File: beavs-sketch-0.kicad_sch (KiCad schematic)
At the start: 26 parts, among them J1 USB_C_Receptacle_USB2.0_16P, J10 Conn_01x03, J11 Conn_01x03, J2 Conn_Coaxial, J3 Micro_SD_Card_Det2, J4 Conn_Coaxial, J5 Conn_01x02, J6 Conn_01x03, J7 Conn_01x03, J8 Conn_01x03, J9 Conn_01x03, U1 RP2040, U2 W25Q128JVS, U3 MS5607-02BA, U4 RFM95W-915S2, U5 MAX-M10S, Y1 Crystal_GND24

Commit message: do some schematic work
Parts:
- removed C1, C2: C_Small, symbol Device:C_Small
- removed J10, J11, J6, J7, J8, J9: Conn_01x03, Connector_JST:JST_XH_B3B-XH-AM_1x03_P2.50mm_Vertical, symbol Connector_Generic:Conn_01x03
- removed J2: Conn_Coaxial, Connector_Coaxial:U.FL_Molex_MCRF_73412-0110_Vertical, symbol Connector:Conn_Coaxial
- removed J3: Micro_SD_Card_Det2, Connector_Card:microSD_HC_Hirose_DM3AT-SF-PEJM5, symbol Connector:Micro_SD_Card_Det2
- removed R1: 1k, Resistor_SMD:R_0402_1005Metric, symbol Device:R_Small
- removed U1: RP2040, Package_DFN_QFN:QFN-56-1EP_7x7mm_P0.4mm_EP3.2x3.2mm, symbol MCU_RaspberryPi:RP2040
- removed U2: W25Q128JVS, Package_SO:SOIC-8_5.3x5.3mm_P1.27mm, symbol Memory_Flash:W25Q128JVS
- removed U3: MS5607-02BA, Package_LGA:LGA-8_3x5mm_P1.25mm, symbol Sensor_Pressure:MS5607-02BA
- removed U5: MAX-M10S, RF_GPS:ublox_MAX, symbol RF_GPS:MAX-M10S
- removed Y1: Crystal_GND24, Crystal:Crystal_SMD_Abracon_ABM8AIG-4Pin_3.2x2.5mm, symbol Device:Crystal_GND24
- added J3: Conn_01x02, Connector_AMASS:AMASS_XT30UPB-F_1x02_P5.0mm_Vertical, symbol Connector_Generic:Conn_01x02
- added Q2: SiS427EDN, Package_SO:Vishay_PowerPAK_1212-8_Single, symbol beavs-symbols:SiS427EDN
- added R2: R_Small, Resistor_SMD:R_0402_1005Metric, symbol Device:R_Small
- added R3, R5: 5.1k, Resistor_SMD:R_0402_1005Metric, symbol Device:R_Small
- added U7: AMS1117-3.3, Package_TO_SOT_SMD:SOT-223-3_TabPin2, symbol Regulator_Linear:AMS1117-3.3
- added U8: AMS1117-5.0, Package_TO_SOT_SMD:SOT-223-3_TabPin2, symbol Regulator_Linear:AMS1117-5.0
- J5: footprint Connector_JST:JST_XH_S2B-XH-A-1_1x02_P2.50mm_Horizontal -> Connector_JST:JST_XH_B2B-XH-A_1x02_P2.50mm_Vertical
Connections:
- net GND: now also J1.A1 (GND), J1.A12 (GND), J1.B1 (GND), J1.B12 (GND), J1.S1 (SHIELD), J3.2 (Pin_2), R2.2, R3.2, R5.2
- net at J1.A5 (CC1): now also R3.1
- net mcu/USB_D+: now reaches J1.A6 (D+)
- net mcu/USB_D+: now also J1.B6 (D+)
- net mcu/USB_D-: now reaches J1.A7 (D-)
- net mcu/USB_D-: now also J1.B7 (D-)
- net at J1.B5 (CC2): now also R5.1
- new net: J3.1 (Pin_1), Q2.5 (D)
- new net: Q2.4 (G), R2.1
- new net +BATT: Q2.1 (S), Q2.2 (S), Q2.3 (S)
- no-connect marks 7 -> 3
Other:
- added sheet SD Card (sd-card.kicad_sch)
- added sheet Sensors (sensors.kicad_sch)
- added sheet mcu (mcu.kicad_sch)
- added sheet servos (servos.kicad_sch)

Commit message: add 3d models and do other stuff
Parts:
- removed J4: Conn_Coaxial, Connector_Coaxial:U.FL_Molex_MCRF_73412-0110_Vertical, symbol Connector:Conn_Coaxial
- removed U4: RFM95W-915S2, RF_Module:HOPERF_RFM9XW_SMD, symbol RF_Module:RFM95W-915S2
- added C15, C18: 10u, Capacitor_SMD:C_0603_1608Metric, symbol Device:C_Small
- added C16, C17: 22u, Capacitor_SMD:C_0603_1608Metric, symbol Device:C_Small
- added D7, D8: D_Schottky, Diode_SMD:D_SOD-123, symbol Device:D_Schottky
- added R6, R7: R_Small, Resistor_SMD:R_0402_1005Metric, symbol Device:R_Small
- added U15: SN74LVC8T245, Package_SO:TSSOP-24_4.4x7.8mm_P0.65mm, symbol Logic_LevelTranslator:SN74LVC8T245
- added U16: SRV05-4, Package_TO_SOT_SMD:SOT-23-6, symbol Power_Protection:SRV05-4
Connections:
- net +3V3: now also U7.2 (VO), C17.1, U15.1 (V_{CCA})
- net +5V: now also U8.2 (VO), C16.1, U15.23 (V_{CCB}), U15.24 (V_{CCB})
- net +BATT: now also D7.2 (A), R6.1
- net ARM_SWITCH: now also J5.2 (Pin_2); no longer J5.1 (Pin_1)
- net GND: now also J5.1 (Pin_1), U7.1 (GND), U8.1 (GND), C15.2, C16.2, C17.2, C18.2, R7.2, U15.11 (GND), U15.12 (GND), U15.13 (GND); no longer J5.2 (Pin_2)
- net at U8.3 (VI): now also U7.3 (VI), C15.1, C18.1, D7.1 (K), D8.1 (K)
- net VBUS: now reaches J1.A4 (VBUS), J1.A9 (VBUS), J1.B4 (VBUS), J1.B9 (VBUS)
- net VBUS: now also D8.2 (A)
- net at D1.3 (DIN): now also U15.15 (B7)
- new net mcu/BATTERY_SENSE: R6.2, R7.1
- new net mcu/M_LED_D: U15.9 (A7)
- new net mcu/M_S1: U15.3 (A1)
- new net mcu/M_S2: U15.4 (A2)
- new net mcu/M_S3: U15.5 (A3)
- new net mcu/M_S4: U15.6 (A4)
- new net mcu/M_S5: U15.7 (A5)
- new net mcu/M_S6: U15.8 (A6)
- new net servos/S1: U15.21 (B1)
- new net servos/S2: U15.20 (B2)
- new net servos/S3: U15.19 (B3)
- new net servos/S4: U15.18 (B4)
- new net servos/S5: U15.17 (B5)
- new net servos/S6: U15.16 (B6)
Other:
- added sheet Radio (radio.kicad_sch)
- sheet mcu ports: added ARM_SWITCH, BARO_CS, BATTERY_SENSE, IMU_CS, MISO, MOSI, M_LED_D, M_S1, M_S2, M_S3, M_S4, M_S5, M_S6, RADIO_CS, RADIO_D0, RADIO_RESET, SCK, SCL, SDA; removed none
- sheet servos ports: added S1, S2, S3, S4, S5, S6, SCL, SDA; removed none
- moved on the sheet: D1, D2, D3, D4, D5, D6, J1, J3, J5, Q2, R2, R3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

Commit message: add some TVS diodes
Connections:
- net +5V: now also U16.5 (VP)
- net GND: now also U16.2 (VN)
- net servos/S1: now also U16.1 (IO1)
- net servos/S2: now also U16.3 (IO2)
- net servos/S3: now also U16.4 (IO3)
- net servos/S4: now also U16.6 (IO4)
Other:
- moved on the sheet: C15, C16, C17, C18, D7, D8, U16, U7, U8

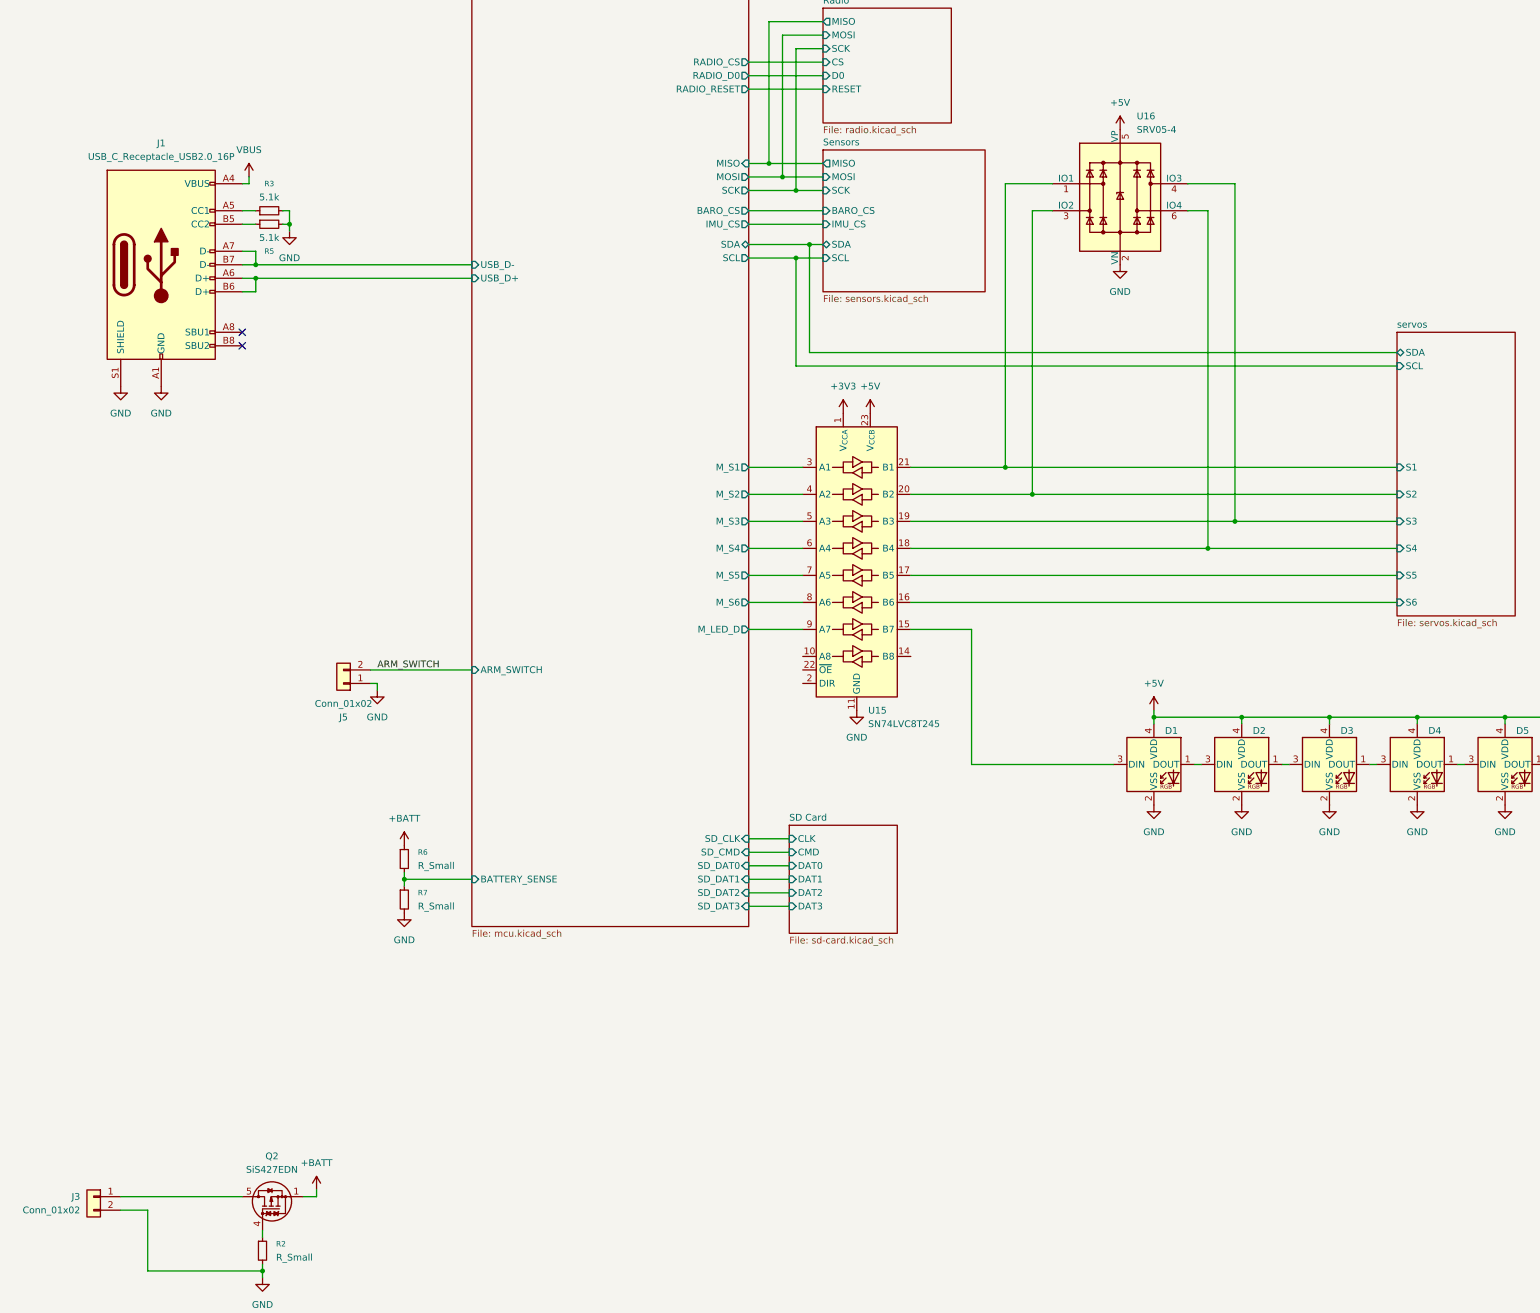
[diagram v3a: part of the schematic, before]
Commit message: update schematics and add 3d models
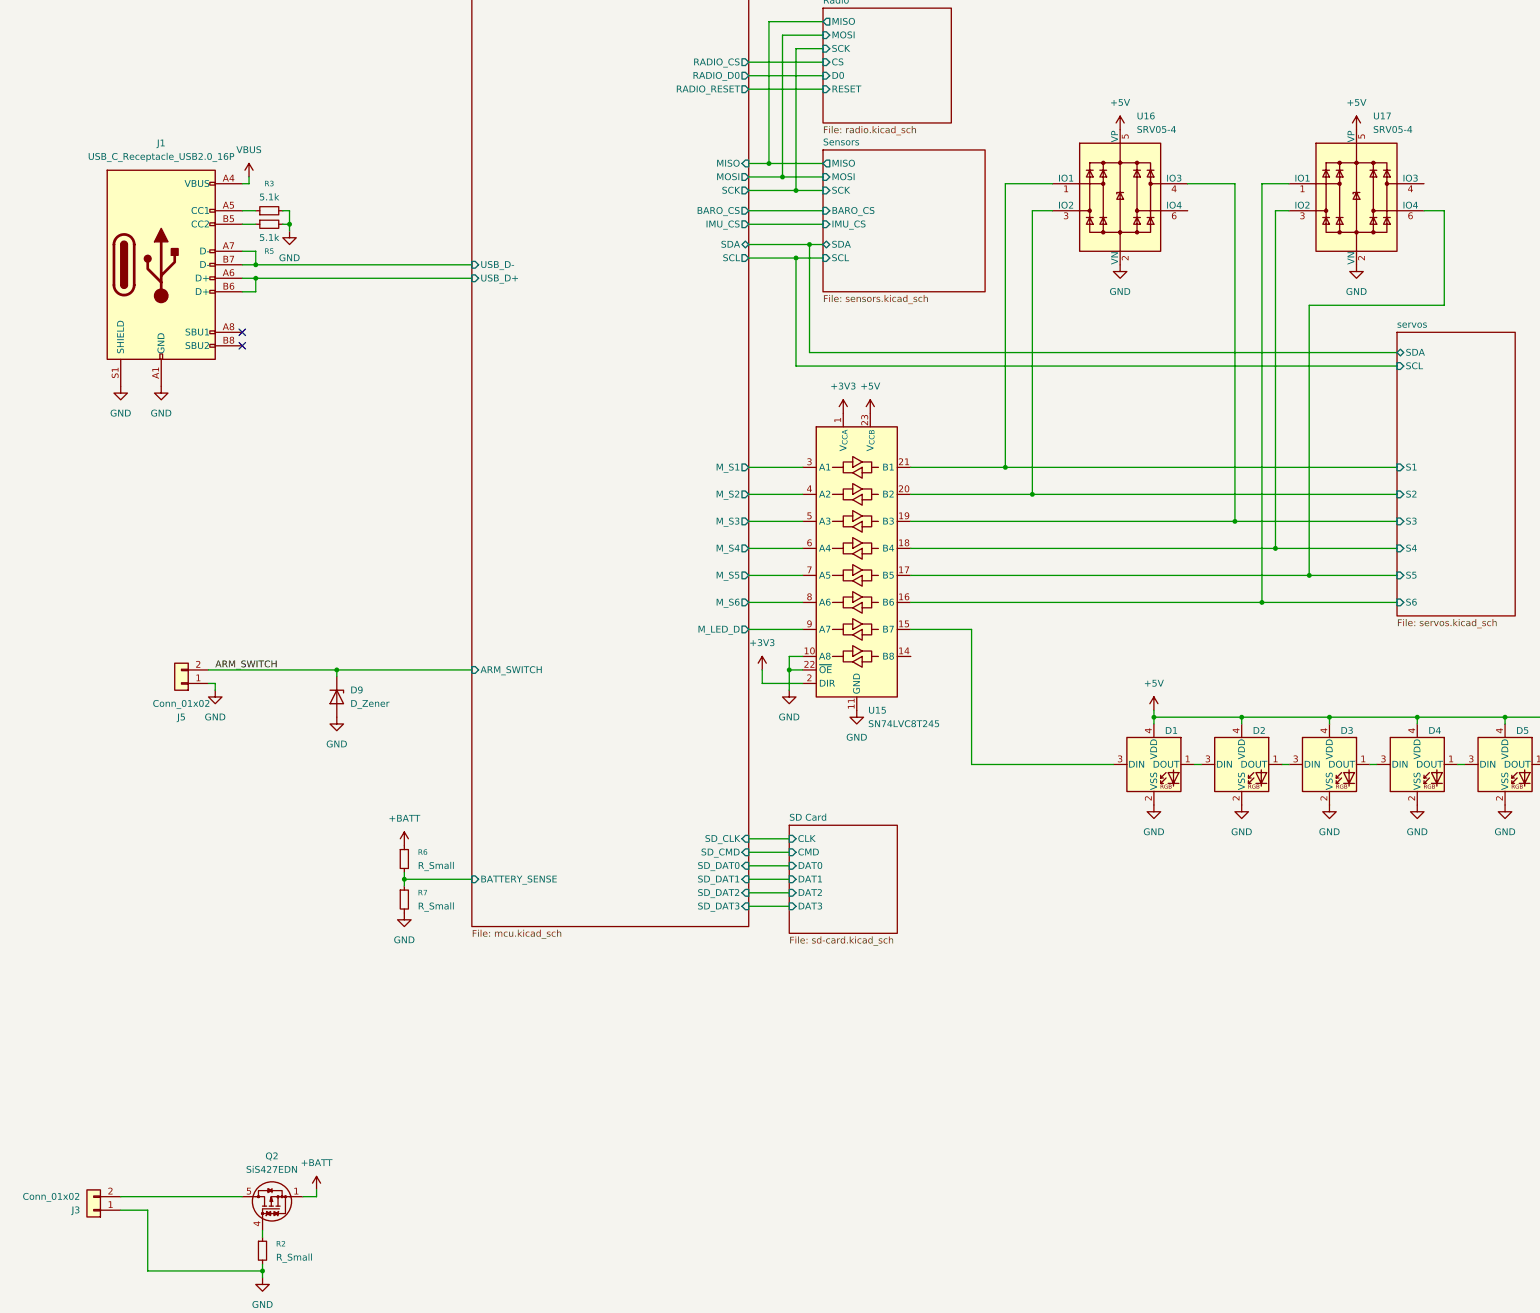
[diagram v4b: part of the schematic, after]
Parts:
- added D9: D_Zener, Diode_SMD:D_SOD-323, symbol Device:D_Zener
- added U17: SRV05-4, Package_TO_SOT_SMD:SOT-23-6, symbol Power_Protection:SRV05-4
- C15, C18: LCSC (none) -> C19702
- C16, C17: LCSC (none) -> C59461
- D7, D8: LCSC (none) -> C8598
- J1: LCSC (none) -> C2988369
- J3: footprint Connector_AMASS:AMASS_XT30UPB-F_1x02_P5.0mm_Vertical -> Connector_AMASS:AMASS_XT30UPB-M_1x02_P5.0mm_Vertical
- J5: footprint Connector_JST:JST_XH_B2B-XH-A_1x02_P2.50mm_Vertical -> Connector_JST:JST_PH_B2B-PH-K_1x02_P2.00mm_Vertical
- R3, R5: LCSC (none) -> C25905
- U15: LCSC (none) -> C27643
- U16: LCSC (none) -> C7420376
- U7: LCSC (none) -> C6186
- U8: LCSC (none) -> C6187
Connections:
- net +3V3: now also U15.2 (DIR)
- net +5V: now also U17.5 (VP)
- net ARM_SWITCH: now also D9.1 (K)
- net GND: now also J3.1 (Pin_1), U15.10 (A8), U15.22 (~{OE}), D9.2 (A), U17.2 (VN); no longer J3.2 (Pin_2)
- net servos/S4: now also U17.3 (IO2); no longer U16.6 (IO4)
- net servos/S5: now also U17.6 (IO4)
- net servos/S6: now also U17.1 (IO1)
- net at Q2.5 (D): now also J3.2 (Pin_2); no longer J3.1 (Pin_1)
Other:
- moved on the sheet: J3, J5

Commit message: cleanup
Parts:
- added J13: USB_C_Receptacle_USB2.0_16P, Connector_USB:USB_C_Receptacle_G-Switch_GT-USB-7051x, symbol Connector:USB_C_Receptacle_USB2.0_16P
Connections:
- new net: J13.A1 (GND), J13.A12 (GND), J13.B1 (GND), J13.B12 (GND)
- new net: J13.A4 (VBUS), J13.A9 (VBUS), J13.B4 (VBUS), J13.B9 (VBUS)
- no-connect marks 3 -> 4
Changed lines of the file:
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@@
 		(at 81.28 93.98)
 	)
+	(no_connect
+		(at 207.01 152.4)
+	)
 	(wire
 		(pts
@@
 					(unit 1)
 				)
+			)
+		)
+	)
+	(symbol
+		(lib_id "Connector:USB_C_Receptacle_USB2.0_16P")
+		(at 20.32 83.82 0)
+		(unit 1)
+		(exclude_from_sim no)
+		(in_bom yes)
+		(on_board yes)
+		(dnp no)
+		(fields_autoplaced yes)
+		(property "Reference" "J13"
+			(at 20.32 60.96 0)
+			(effects
+				(font
+					(size 1.27 1.27)
+				)
+			)
+		)
+		(property "Value" "USB_C_Receptacle_USB2.0_16P"
+			(at 20.32 63.5 0)
+			(effects
+				(font
+					(size 1.27 1.27)
+				)
+			)
+		)
+		(property "Footprint" "Connector_USB:USB_C_Receptacle_G-Switch_GT-USB-7051x"
+			(at 24.13 83.82 0)
+			(effects
+				(font
+					(size 1.27 1.27)
+				)
+				(hide yes)
+			)
+		)
+		(property "Datasheet" "https://www.usb.org/sites/default/files/documents/usb_type-c.zip"
+			(at 24.13 83.82 0)
+			(effects
+				(font
+					(size 1.27 1.27)
+				)
+				(hide yes)
+			)
+		)
+		(property "Description" "USB 2.0-only 16P Type-C Receptacle connector"
+			(at 20.32 83.82 0)
+			(effects
+				(font
+					(size 1.27 1.27)
+				)
+				(hide yes)
+			)
+		)
+		(pin "A5"
+		)
+		(pin "B5"
+		)
+		(pin "B4"
+		)
+		(pin "B6"
+		)
+		(pin "A12"
+		)
+		(pin "A7"
+		)
+		(pin "S1"
+		)
+		(pin "A8"
+		)
+		(pin "B12"
+		)
+		(pin "A1"
+		)
+		(pin "B7"
+		)
+		(pin "B9"
+		)
+		(pin "B8"
+		)
+		(pin "B1"
+		)
+		(pin "A9"
+		)
+		(pin "A6"
+		)
+		(pin "A4"
+		)
+		(instances
+			(project ""
+				(path "/49232f62-a438-4b3e-9be5-c2b3074d8de1"
+					(reference "J13")
+					(unit 1)
+				)
